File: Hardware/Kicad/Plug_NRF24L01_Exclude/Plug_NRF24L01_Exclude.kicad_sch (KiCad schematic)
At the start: 25 parts, among them J1 Conn_01x07_Socket, J2 Conn_01x08_Socket, Q1 2N7002, Q2 2N7002, Q3 2N7002, SW1 SW_Push, U2 AMS1117-3.3, U3 STM32L412KBTx

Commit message: Corrective changes on the Plug_NRF24L01_Exclude KiCad
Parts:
- removed C1: 1u, Capacitor_SMD:C_0603_1608Metric_Pad1.08x0.95mm_HandSolder, symbol Device:C_Small
- removed U2: AMS1117-3.3, Package_TO_SOT_SMD:SOT-223-3_TabPin2, symbol Regulator_Linear:AMS1117-3.3
- added C2: 470p, Capacitor_SMD:C_0603_1608Metric_Pad1.08x0.95mm_HandSolder, symbol Device:C_Small
- added C3, C4, C5, C6: 100n, Capacitor_SMD:C_0603_1608Metric_Pad1.08x0.95mm_HandSolder, symbol Device:C_Small
- added D2: LED, Diode_SMD:D_0603_1608Metric_Pad1.05x0.95mm_HandSolder, symbol Device:LED_Small
- added J2: Conn_02x07_Odd_Even, Connector_PinHeader_1.27mm:PinHeader_2x07_P1.27mm_Vertical_SMD, symbol Connector_Generic:Conn_02x07_Odd_Even
- added Q3 (x2): 2N7002, Package_TO_SOT_SMD:SOT-23, symbol Transistor_FET:2N7002
- added R3: 1k, Resistor_SMD:R_0603_1608Metric_Pad0.98x0.95mm_HandSolder, symbol Device:R_Small
- added R7 (x2), R8 (x2): 10k, Resistor_SMD:R_0603_1608Metric_Pad0.98x0.95mm_HandSolder, symbol Device:R_Small
- added U2: MIC5219-3.3YMM, Package_SO:MSOP-8_3x3mm_P0.65mm, symbol Regulator_Linear:MIC5219-3.3YMM
- C2: value 1u -> 2.2u
- J1: footprint Connector_PinSocket_1.00mm:PinSocket_1x07_P1.00mm_Vertical -> Connector_JST:JST_EH_B7B-EH-A_1x07_P2.50mm_Vertical
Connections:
- net +3.3V: now also C4.1, C5.1, C6.1, D2.2 (A), J2.3 (Pin_3), Q3.1 (G), Q3.1 (G), R7.1, R7.1, U2.3 (OUT)
- net +5V: now also R8.1, R8.1, U2.2 (IN)
- net GND: now also C2.2, C3.1, C4.2, C5.2, C6.2, J2.11 (Pin_11), J2.5 (Pin_5), J2.7 (Pin_7), R3.2, U2.5 (GND), U2.6 (GND), U2.7 (GND), U2.8 (GND)
- net Player1_LED: now also U3.20 (PA10); no longer U3.24 (PA14)
- net SPI_Clock: now also U3.6 (PA0); no longer U3.9 (PA3)
- net SPI_Digital_Input: now also U3.12 (PA6); no longer U3.8 (PA2)
- net SWDIO: now reaches U3.23 (PA13)
- net SWDIO: now also J2.4 (Pin_4)
- net Serial_Data2_SNES: now reaches U3.28 (PB5)
- net Serial_Data2_SNES: now also J1.5 (Pin_5), Q3.3 (D), R8.2
- net IOBit_SNES: now reaches U3.30 (PB7)
- net IOBit_SNES: now also J1.6 (Pin_6), Q3.3 (D), R8.2
- net NRST: now reaches U3.4 (NRST)
- net NRST: now also C3.2, J2.12 (Pin_12)
- net Serial_Data_SNES renamed Serial_Data1_SNES
- net Serial_Data_STM32 renamed Serial_Data1_STM32
- new net: C2.1, U2.4 (BP)
- new net: D2.1 (K), R3.1
- new net IOBit_STM32: Q3.2 (S), R7.2
- new net SWDCK: J2.6 (Pin_6), U3.24 (PA14)
- new net Serial_Data2_STM32: Q3.2 (S), R7.2
- new net USART2_RX: J2.13 (Pin_13), U3.9 (PA3)
- new net USART2_TX: J2.14 (Pin_14), U3.8 (PA2)
- no-connect marks 19 -> 17
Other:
- note added: "MIC5219-3.3YMM 5 to 3.3"
- note added: "SWD Connector"
- note removed: "AMS1117-3.3"
- moved on the sheet: C2, D2, D3, H1, H2, H3, H4, J1, J2, Q1, Q2, Q3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

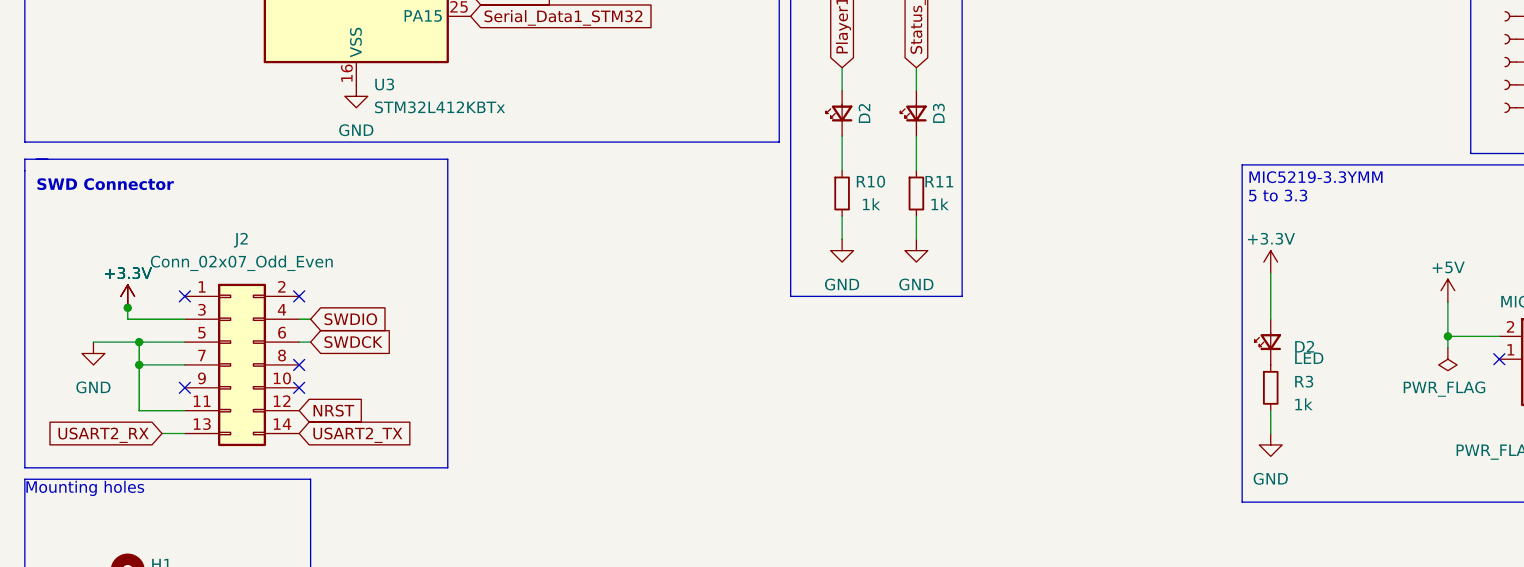
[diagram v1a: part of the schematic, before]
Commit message: Updated Plug_NRF24L01_Include Schematic & Include (Added new components and modified footprints). Fixed some errors on NRF24L01_Exclude.
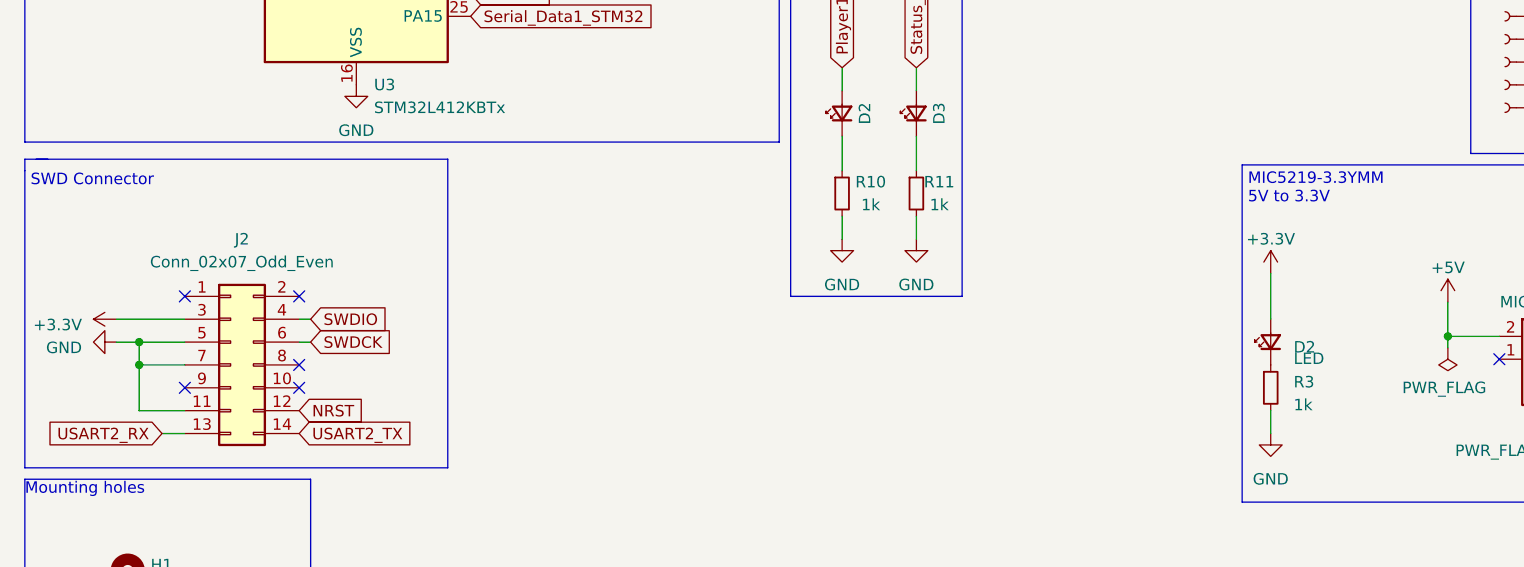
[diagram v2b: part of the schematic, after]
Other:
- note added: "MIC5219-3.3YMM 5V to 3.3V"
- note removed: "MIC5219-3.3YMM 5 to 3.3"
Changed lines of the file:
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@@
   (junction (at 259.08 101.6) (diameter 0) (color 0 0 0 0)
-  )
-  (junction (at 27.94 107.315) (diameter 0) (color 0 0 0 0)
   )
   (junction (at 20.32 141.605) (diameter 0) (color 0 0 0 0)
@@
     (stroke (width 0) (type default))
   )
-  (wire (pts (xy 24.13 111.125) (xy 29.21 111.125))
+  (wire (pts (xy 26.67 111.125) (xy 29.21 111.125))
     (stroke (width 0) (type default))
   )
@@
     (stroke (width 0) (type default))
   )
-  (wire (pts (xy 27.94 108.585) (xy 27.94 107.315))
-    (stroke (width 0) (type default))
-  )
   (wire (pts (xy 237.49 80.01) (xy 240.03 80.01))
     (stroke (width 0) (type default))
@@
     (stroke (width 0) (type default))
   )
-  (wire (pts (xy 34.29 108.585) (xy 27.94 108.585))
+  (wire (pts (xy 34.29 108.585) (xy 26.67 108.585))
     (stroke (width 0) (type default))
   )
@@
     (stroke (width 0) (type default))
   )
-  (text "MIC5219-3.3YMM\n5 to 3.3\n" (at 152.4 95.885 0)
+  (text "MIC5219-3.3YMM\n5V to 3.3V" (at 152.4 95.885 0)
     (effects (font (size 1.27 1.27)) (justify left bottom))
   )
@@
     (effects (font (size 1.27 1.27)) (justify left bottom))
   )
-  (text "SWD Connector" (at 17.78 94.615 0)
-    (effects (font (size 1.27 1.27) (thickness 0.254) bold) (justify left bottom))
-  )
   (text "Level Shifter\n" (at 215.9 16.51 0)
     (effects (font (size 1.27 1.27)) (justify left bottom))
@@
   )
   (text "System LEDs\n" (at 102.87 64.77 0)
+    (effects (font (size 1.27 1.27)) (justify left bottom))
+  )
+  (text "SWD Connector" (at 17.145 93.98 0)
     (effects (font (size 1.27 1.27)) (justify left bottom))
   )
@@
     )
   )
-  (symbol (lib_id "power:GND") (at 24.13 111.125 0) (unit 1)
-    (in_bom yes) (on_board yes) (dnp no) (fields_autoplaced)
-    (property "Reference" "#PWR04" (at 24.13 117.475 0)
-      (effects (font (size 1.27 1.27)) hide)
-    )
-    (property "Value" "GND" (at 24.13 116.205 0)
-      (effects (font (size 1.27 1.27)))
-    )
-    (property "Footprint" "" (at 24.13 111.125 0)
-      (effects (font (size 1.27 1.27)) hide)
-    )
-    (property "Datasheet" "" (at 24.13 111.125 0)
+  (symbol (lib_id "power:GND") (at 26.67 111.125 270) (unit 1)
+    (in_bom yes) (on_board yes) (dnp no) (fields_autoplaced)
+    (property "Reference" "#PWR04" (at 20.32 111.125 0)
+      (effects (font (size 1.27 1.27)) hide)
+    )
+    (property "Value" "GND" (at 22.86 111.76 90)
+      (effects (font (size 1.27 1.27)) (justify right))
+    )
+    (property "Footprint" "" (at 26.67 111.125 0)
+      (effects (font (size 1.27 1.27)) hide)
+    )
+    (property "Datasheet" "" (at 26.67 111.125 0)
       (effects (font (size 1.27 1.27)) hide)
     )
@@
     )
   )
-  (symbol (lib_id "power:+3.3V") (at 27.94 107.315 0) (unit 1)
-    (in_bom yes) (on_board yes) (dnp no) (fields_autoplaced)
-    (property "Reference" "#PWR08" (at 27.94 111.125 0)
-      (effects (font (size 1.27 1.27)) hide)
-    )
-    (property "Value" "+3.3V" (at 27.94 103.505 0)
-      (effects (font (size 1.27 1.27)))
-    )
-    (property "Footprint" "" (at 27.94 107.315 0)
-      (effects (font (size 1.27 1.27)) hide)
-    )
-    (property "Datasheet" "" (at 27.94 107.315 0)
-      (effects (font (size 1.27 1.27)) hide)
-    )
-    (pin "1")
-    (instances
-      (project "Controler_NRF24L01_Exclude"
-        (path "/76ef48f1-60b7-4c4b-a0ce-73b6af33b115"
-          (reference "#PWR08") (unit 1)
-        )
-      )
-      (project "PCBschematic"
-        (path "/cc300af8-7dc6-4303-a7a3-6c9320b23fa8"
-          (reference "#PWR020") (unit 1)
-        )
-      )
-      (project "Plug_NRF24L01_Exclude"
-        (path "/e27c4aed-f26e-4205-8842-b91be8be392b"
-          (reference "#PWR09") (unit 1)
-        )
-      )
-    )
-  )
-  (symbol (lib_id "power:+3.3V") (at 27.94 107.315 0) (unit 1)
-    (in_bom yes) (on_board yes) (dnp no) (fields_autoplaced)
-    (property "Reference" "#PWR06" (at 27.94 111.125 0)
-      (effects (font (size 1.27 1.27)) hide)
-    )
-    (property "Value" "+3.3V" (at 27.94 103.505 0)
-      (effects (font (size 1.27 1.27)))
-    )
-    (property "Footprint" "" (at 27.94 107.315 0)
-      (effects (font (size 1.27 1.27)) hide)
-    )
-    (property "Datasheet" "" (at 27.94 107.315 0)
-      (effects (font (size 1.27 1.27)) hide)
-    )
+  (symbol (lib_id "power:+3.3V") (at 26.67 108.585 90) (unit 1)
+    (in_bom yes) (on_board yes) (dnp no) (fields_autoplaced)
+    (property "Reference" "#PWR06" (at 30.48 108.585 0)
+      (effects (font (size 1.27 1.27)) hide)
+    )
+    (property "Value" "+3.3V" (at 22.86 109.22 90)
+      (effects (font (size 1.27 1.27)) (justify left))
+    )
+    (property "Footprint" "" (at 26.67 108.585 0)
+      (effects (font (size 1.27 1.27)) hide)
+    )
+    (property "Datasheet" "" (at 26.67 108.585 0)
+      (effects (font (size 1.27 1.27)) hide)
+    )

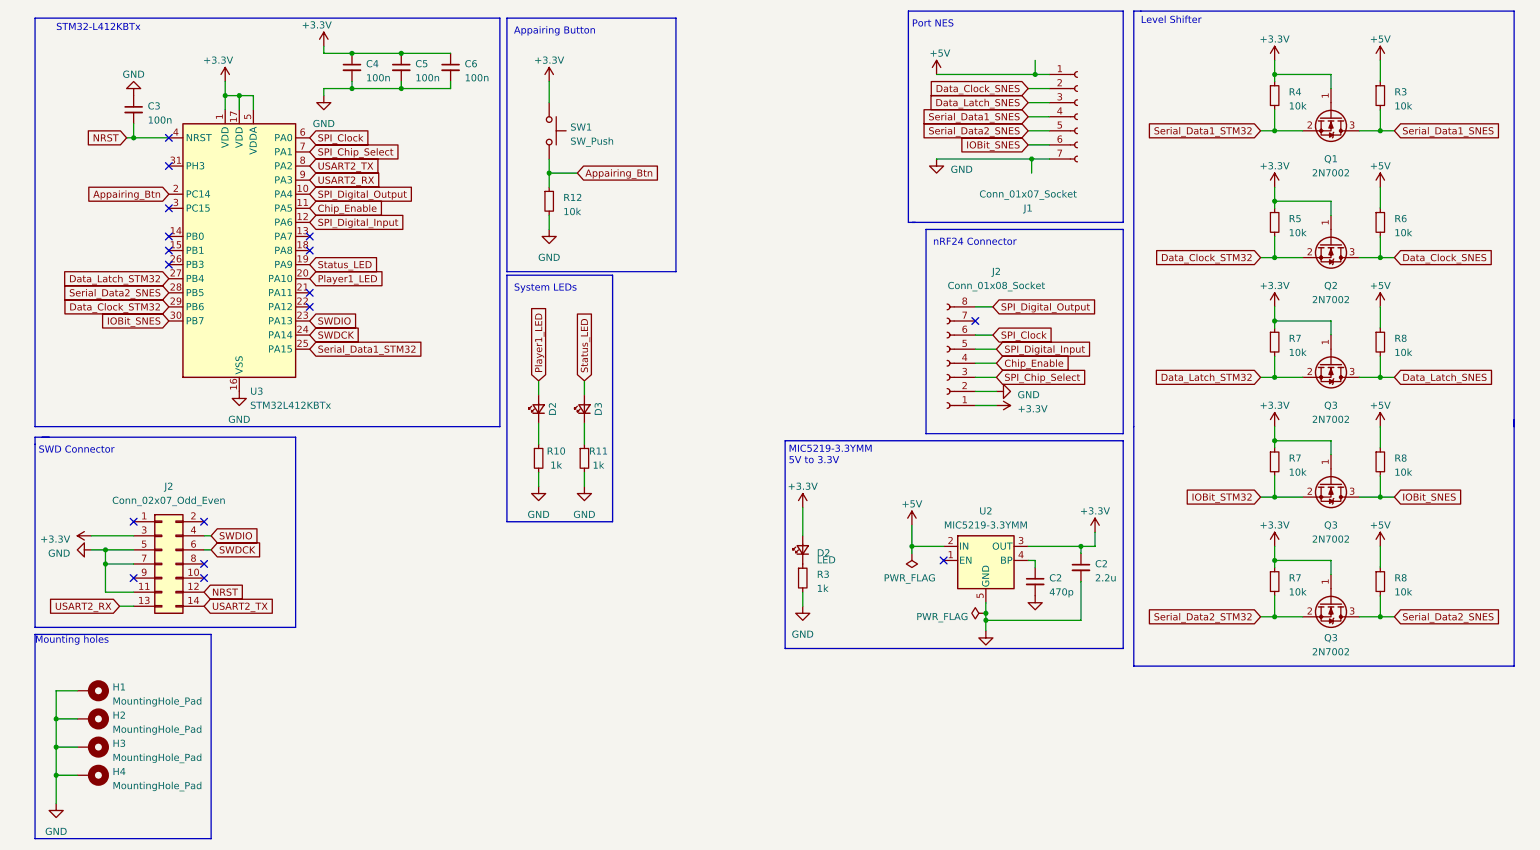
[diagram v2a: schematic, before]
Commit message: Updated Plug_NRF24L01_Exclude (Version 1.0) - Schematic (New pins assignment / New buttons) - PCB (Completed Routing V1)
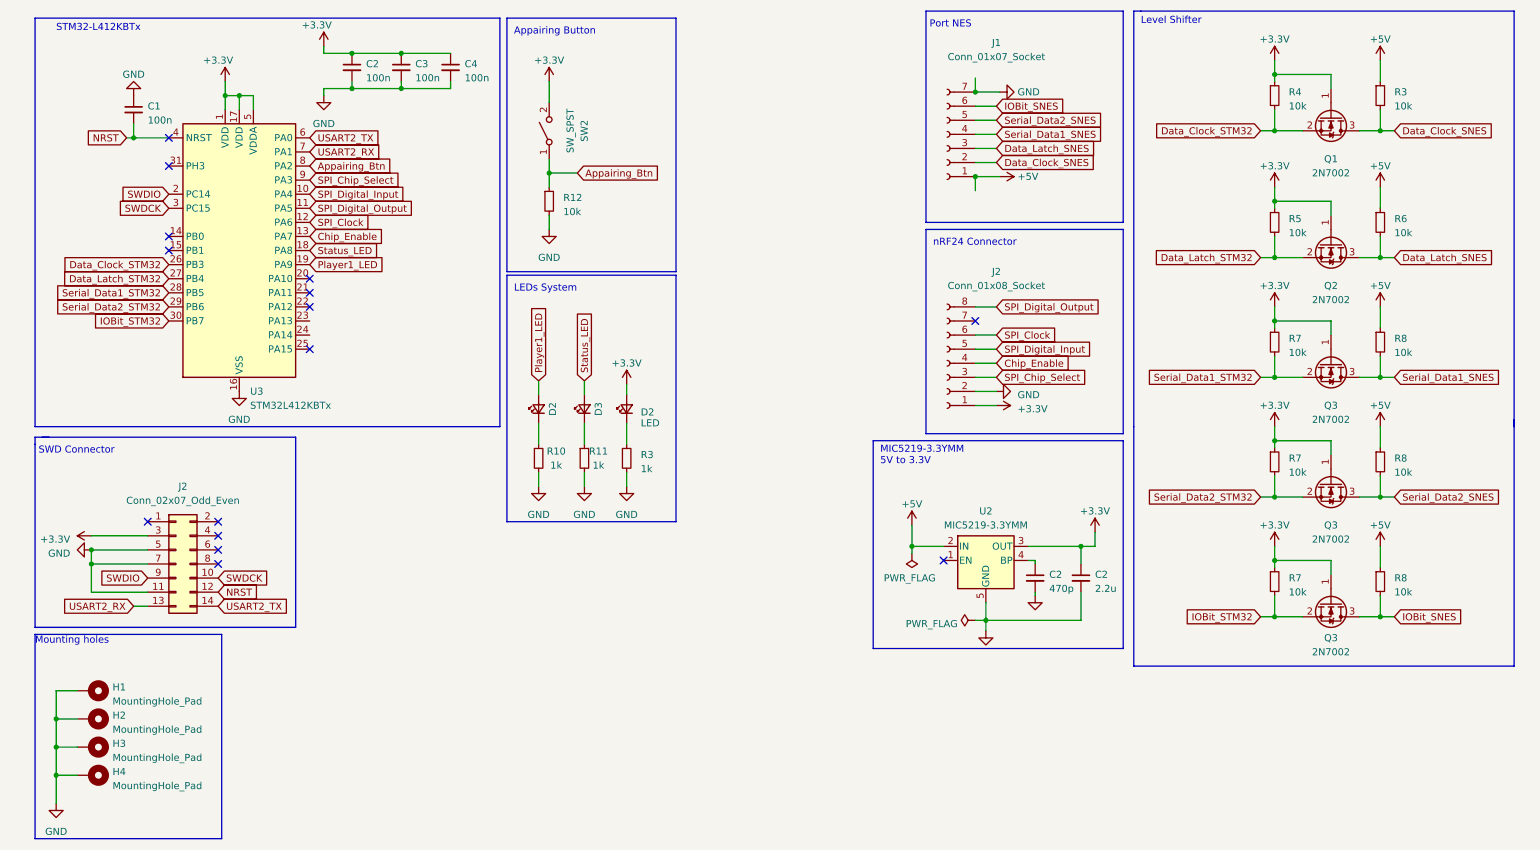
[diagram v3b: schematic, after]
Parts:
- removed SW1: SW_Push, Button_Switch_SMD:SW_Push_1P1T_NO_6x6mm_H9.5mm, symbol Switch:SW_Push
- added SW2: SW_SPST, Button_Switch_SMD:SW_SPST_B3S-1000, symbol Switch:SW_SPST
- renumbered C3 to C1, C4 to C2, C5 to C3, C6 to C4
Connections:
- net +3.3V: now also SW2.2 (B)
- net Appairing_Btn: now also U3.8 (PA2), SW2.1 (A); no longer U3.2 (PC14)
- net Chip_Enable: now also U3.13 (PA7); no longer U3.11 (PA5)
- net Data_Clock_SNES: now also Q1.3 (D), R3.2; no longer Q2.3 (D), R6.2
- net Data_Clock_STM32: now also Q1.2 (S), R4.2, U3.26 (PB3); no longer Q2.2 (S), R5.2, U3.29 (PB6)
- net Data_Latch_SNES: now also Q2.3 (D), R6.2; no longer Q3.3 (D), R8.2
- net Data_Latch_STM32: now also Q2.2 (S), R5.2; no longer Q3.2 (S), R7.2
- net IOBit_SNES: now also Q3.3 (D), R8.2; no longer Q3.3 (D), R8.2, U3.30 (PB7)
- net IOBit_STM32: now also Q3.2 (S), R7.2, U3.30 (PB7); no longer Q3.2 (S), R7.2
- net Player1_LED: now also U3.19 (PA9); no longer U3.20 (PA10)
- net SPI_Chip_Select: now also U3.9 (PA3); no longer U3.7 (PA1)
- net SPI_Clock: now also U3.12 (PA6); no longer U3.6 (PA0)
- net SPI_Digital_Input: now also U3.10 (PA4); no longer U3.12 (PA6)
- net SPI_Digital_Output: now also U3.11 (PA5); no longer U3.10 (PA4)
- net SWDCK: now also J2.10 (Pin_10), U3.3 (PC15); no longer J2.6 (Pin_6), U3.24 (PA14)
- net SWDIO: now also J2.9 (Pin_9), U3.2 (PC14); no longer J2.4 (Pin_4), U3.23 (PA13)
- net Serial_Data1_SNES: now also Q3.3 (D), R8.2; no longer Q1.3 (D), R3.2
- net Serial_Data1_STM32: now also Q3.2 (S), R7.2, U3.28 (PB5); no longer Q1.2 (S), R4.2, U3.25 (PA15)
- net Serial_Data2_SNES: now also Q3.3 (D), R8.2; no longer Q3.3 (D), R8.2, U3.28 (PB5)
- net Serial_Data2_STM32: now also Q3.2 (S), R7.2, U3.29 (PB6); no longer Q3.2 (S), R7.2
- net Status_LED: now also U3.18 (PA8); no longer U3.19 (PA9)
- net USART2_RX: now also U3.7 (PA1); no longer U3.9 (PA3)
- net USART2_TX: now also U3.6 (PA0); no longer U3.8 (PA2)
- no-connect marks 17 -> 15
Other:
- note added: "LEDs System"
- note removed: "System LEDs"
- moved on the sheet: C2, D2, J1, J2, R3
